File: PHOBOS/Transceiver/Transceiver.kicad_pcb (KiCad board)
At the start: 2 copper layers, 18 parts, among them J1 Conn_01x06, J2 Conn_Coaxial, U1 SX1280IMLTRT, Y1 C1E-52.000-10-1012-X-M

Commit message: Initial PCB layout updated.
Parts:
- J2: moved to B.Cu
- moved L4 31.8 mm to (143.6, 97.8), turned to 180 degrees
- moved R15 28.7 mm to (140.6, 94.4), turned to -90 degrees
- moved C8 28.7 mm to (142.4, 94.8), turned to 180 degrees
- moved C9 28.1 mm to (142.4, 95.8), turned to 180 degrees
- moved C10 25.3 mm to (146.0, 97.8), turned to -90 degrees
- moved C6 23.3 mm to (147.0, 90.0), turned to 90 degrees
- moved J1 23.2 mm to (153.9, 101.2), turned to -90 degrees
- moved C0 22.6 mm to (149.4, 94.4), turned to -90 degrees
- moved L1 19.6 mm to (151.2, 93.8)
- moved J2 19.2 mm to (159.0, 93.8), turned to 180 degrees
- moved C1 19.0 mm to (153.0, 94.4), turned to -90 degrees
- moved C2 15.7 mm to (156.6, 94.4), turned to -90 degrees
- moved L2 15.5 mm to (154.8, 93.8)
- moved C5 14.9 mm to (148.0, 90.0), turned to 90 degrees
- moved C3 12.6 mm to (158.4, 93.8)
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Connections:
- net Net-(J2-In) renamed /ANTENNA
- net Net-(U1-DCC_FB) renamed /DCC_FB
- net Net-(U1-DCC_SW) renamed /DCC_SW
- net Net-(U1-RFIO) renamed /RFIO
- net Net-(U1-VBAT_IO) renamed /VBAT_IO
- net Net-(U1-VR_PA) renamed /VR_PA
- net Net-(U1-XTA) renamed /XTA
- net Net-(U1-XTB) renamed /XTB
- C10 pad 1: Net-(U1-VBAT) -> VDD
- J1 pad 1: VDD -> /NSS
- J1 pad 5: /NSS -> VDD
- U1 pad 15: Net-(U1-VBAT) -> VDD
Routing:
- net VDD: track 0.00 -> 15.8 mm, vias 0 -> 2
- net /DCC_FB: track 0.00 -> 11.0 mm, vias 0 -> 2
- net /NSS: track 0.00 -> 10.0 mm
- net /SCK: track 0.00 -> 7.88 mm
- net /MOSI: track 0.00 -> 6.02 mm
- net /MISO: track 0.00 -> 5.62 mm
- net GND: track 0.00 -> 4.15 mm, vias 0 -> 1
- net /VBAT_IO: track 0.00 -> 4.05 mm
- net Net-(C2-Pad1): track 0.00 -> 3.69 mm
- net Net-(C1-Pad1): track 0.00 -> 3.68 mm
- net /XTA: track 0.00 -> 3.19 mm
- net /RFIO: track 0.00 -> 2.50 mm
- net /DCC_SW: track 0.00 -> 2.14 mm
- net /XTB: track 0.00 -> 1.95 mm
- net /VR_PA: track 0.00 -> 1.61 mm
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- added copper zone on B.Cu, net GND
- added copper zone on F.Cu, net GND
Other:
- board outline added: 24.2 x 15.6 mm

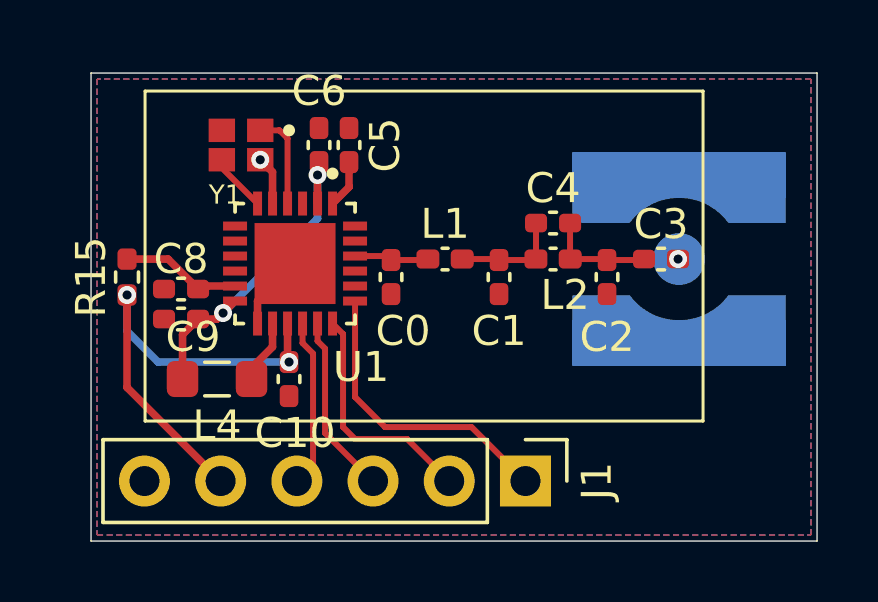
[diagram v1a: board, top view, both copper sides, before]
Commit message: Phobos Budget outline
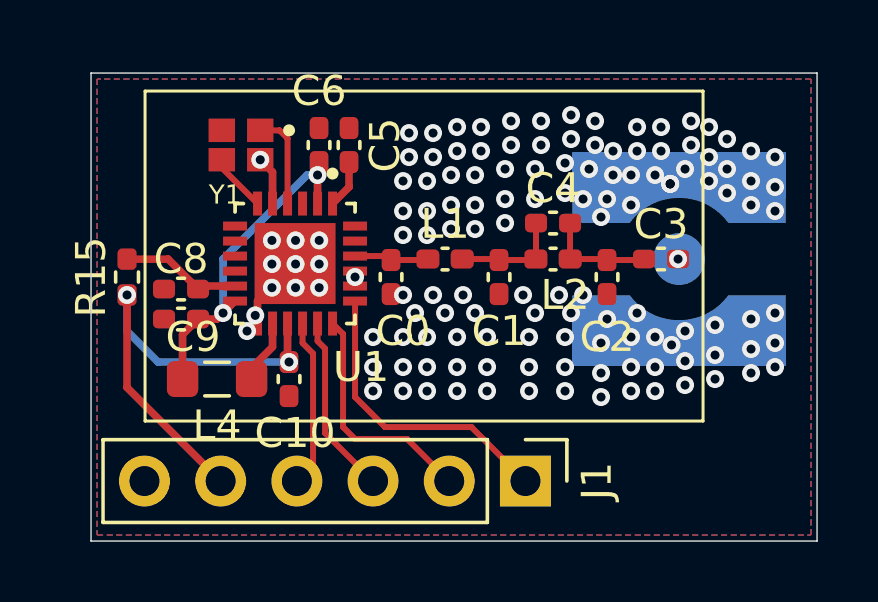
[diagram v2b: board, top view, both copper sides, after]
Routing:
- net GND: vias 1 -> 134

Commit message: design blocks tested. connectors added
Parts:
- removed J1: Conn_01x06, Connector_PinHeader_2.54mm:PinHeader_1x06_P2.54mm_Vertical
- J2: footprint Connector_Coaxial:SMA_Amphenol_132134-10_Vertical -> SMA_J_P_GF_RA_SM1:SAMTEC_SMA-J-P-GF-RA-SM1
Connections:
- net VDD renamed +3.3V
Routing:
- net /NSS: track 10.0 -> 0.00 mm
- net /SCK: track 7.88 -> 0.00 mm
- net +3.3V: track 15.8 -> 8.33 mm
- net /MOSI: track 6.02 -> 0.00 mm
- net /MISO: track 5.62 -> 0.00 mm
